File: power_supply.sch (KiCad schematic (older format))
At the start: 72 parts, among them IC1 TPS54561DPRT, J2 PJ-202A

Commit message: Started placing main components on PCB. Change of RT battery model and USB flash connector
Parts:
- removed BAT1: BU1632SM, sc606-baseboard-footprints:BU1632SM, symbol sc606-baseboard:BU1632SM
- added BAT1: MS621FE-FL11E, sc606-baseboard-footprints:MS621FE-FL11E, symbol sc606-baseboard:MS621FE-FL11E
- gave numbers to parts that had none: 49
- renumbered C21 to C22, C22 to C23, C23 to C25, C24 to C28, C25 to C29, C26 to C30, D?1 to D2, J2 to J1, L1 to L2, R6 to R12, R7 to R13, R8 to R14, R9 to R15, R3 to R6, R5 to R9

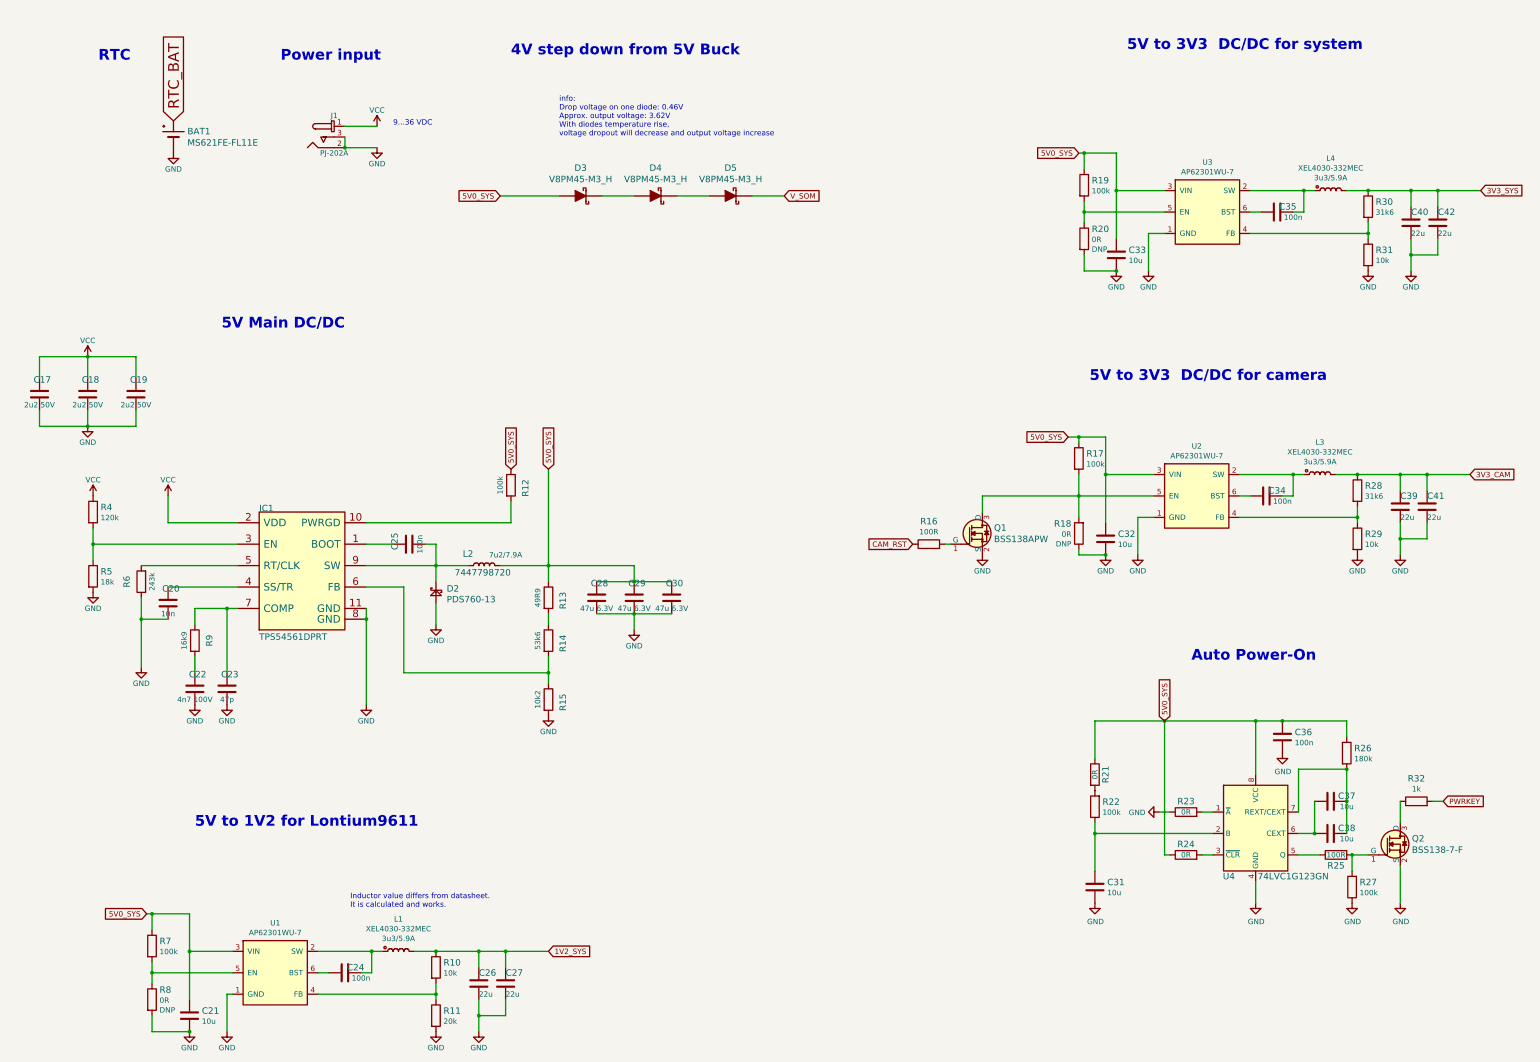
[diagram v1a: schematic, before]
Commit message: Changed USB flash and debug to USB-C. Prepared place for USB PD. Minor modifications of components position
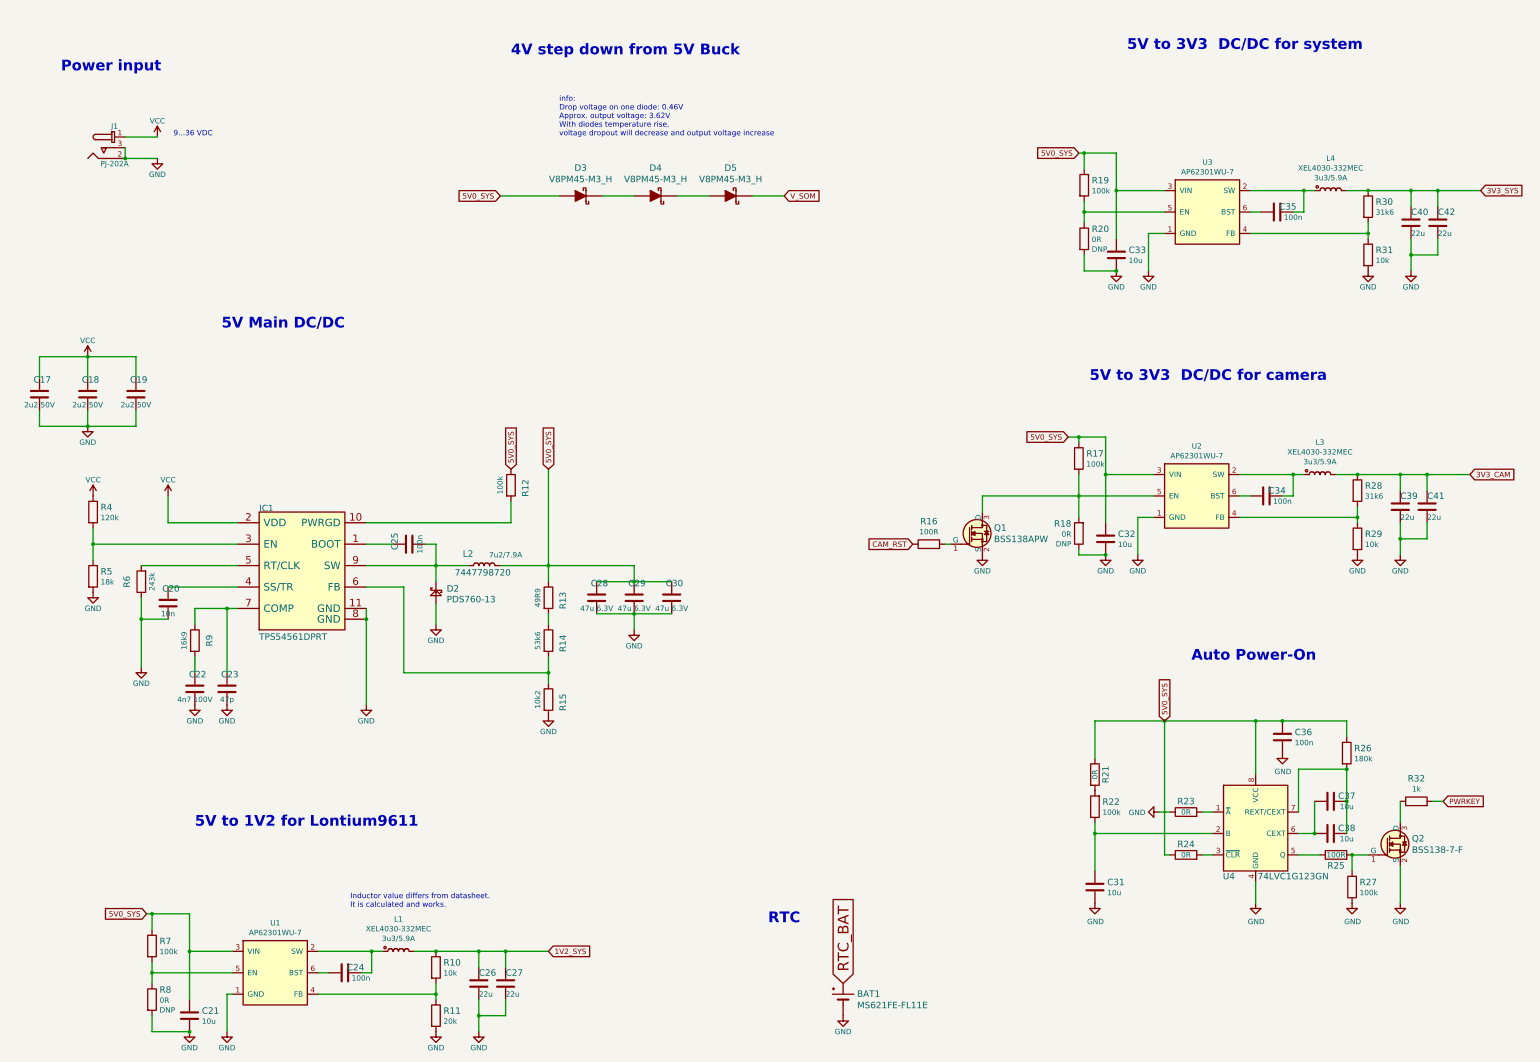
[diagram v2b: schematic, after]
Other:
- moved on the sheet: BAT1, J1
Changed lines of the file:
@@
 $Descr A3 16535 11693
 encoding utf-8
-Sheet 3 8
+Sheet 3 9
 Title ""
 Date "2022-01-04"
@@
 Comment4 ""
 $EndDescr
-Text Notes 1300 1150 0    100  ~ 20
+Text Notes 7550 9200 0    100  ~ 20
 RTC
 Text Notes 2450 3650 0    100  ~ 20
@@
 L sc606-baseboard:GND #PWR025
 U 1 1 623E5A47
-P 2000 2000
-F 0 "#PWR025" H 2000 1750 50  0001 C CNN
-F 1 "GND" H 2000 1850 50  0000 C CNN
-F 2 "" H 2000 2000 50  0001 C CNN
-F 3 "" H 2000 2000 50  0001 C CNN
-	1    2000 2000
-	1    0    0    -1
-$EndComp
-Text GLabel 2000 1700 1    100  Input ~ 0
+P 8250 10050
+F 0 "#PWR025" H 8250 9800 50  0001 C CNN
+F 1 "GND" H 8250 9900 50  0000 C CNN
+F 2 "" H 8250 10050 50  0001 C CNN
+F 3 "" H 8250 10050 50  0001 C CNN
+	1    8250 10050
+	1    0    0    -1
+$EndComp
+Text GLabel 8250 9750 1    100  Input ~ 0
 RTC_BAT
-Text Notes 3000 1150 0    100  ~ 20
+Text Notes 950  1250 0    100  ~ 20
 Power input
 $Comp
 L sc606-baseboard:PJ-202A J1
 U 1 1 623EC1D3
-P 3500 1750
-F 0 "J1" H 3500 1850 50  0000 C CNN
-F 1 "PJ-202A" H 3500 1500 50  0000 C CNN
-F 2 "sc606-baseboard-footprints:Barrel_Jack_5.5mmODx2.1mmID_PJ-202A" H 3700 1950 60  0001 L CNN
-F 3 "https://www.cui.com/product/resource/digikeypdf/pj-202a.pdf" H 3700 2050 60  0001 L CNN
-F 4 "CUI Inc." H 3700 2850 60  0001 L CNN "Manufacturer"
-F 5 "PJ-202A" H 3700 2250 60  0001 L CNN "MPN"
-	1    3500 1750
+P 1450 1850
+F 0 "J1" H 1450 1950 50  0000 C CNN
+F 1 "PJ-202A" H 1450 1600 50  0000 C CNN
+F 2 "sc606-baseboard-footprints:Barrel_Jack_5.5mmODx2.1mmID_PJ-202A" H 1650 2050 60  0001 L CNN
+F 3 "https://www.cui.com/product/resource/digikeypdf/pj-202a.pdf" H 1650 2150 60  0001 L CNN
+F 4 "CUI Inc." H 1650 2950 60  0001 L CNN "Manufacturer"
+F 5 "PJ-202A" H 1650 2350 60  0001 L CNN "MPN"
+	1    1450 1850
 	1    0    0    -1
 $EndComp
@@
 L sc606-baseboard:GND #PWR032
 U 1 1 623ECF5D
-P 3900 1950
-F 0 "#PWR032" H 3900 1700 50  0001 C CNN
-F 1 "GND" H 3900 1800 50  0000 C CNN
-F 2 "" H 3900 1950 50  0001 C CNN
-F 3 "" H 3900 1950 50  0001 C CNN
-	1    3900 1950
-	1    0    0    -1
-$EndComp
-Wire Wire Line
-	3600 1850 3600 1950
-Wire Wire Line
-	3900 1950 3600 1950
-Connection ~ 3600 1950
+P 1850 2050
+F 0 "#PWR032" H 1850 1800 50  0001 C CNN
+F 1 "GND" H 1850 1900 50  0000 C CNN
+F 2 "" H 1850 2050 50  0001 C CNN
+F 3 "" H 1850 2050 50  0001 C CNN
+	1    1850 2050
+	1    0    0    -1
+$EndComp
+Wire Wire Line
+	1550 1950 1550 2050
+Wire Wire Line
+	1850 2050 1550 2050
+Connection ~ 1550 2050
 $Comp
 L sc606-baseboard:VCC #PWR031
 U 1 1 623EE843
-P 3900 1750
-F 0 "#PWR031" H 3900 1600 50  0001 C CNN
-F 1 "VCC" H 3900 1900 50  0000 C CNN
-F 2 "" H 3900 1750 50  0001 C CNN
-F 3 "" H 3900 1750 50  0001 C CNN
-	1    3900 1750
-	1    0    0    -1
-$EndComp
-Wire Wire Line
-	3900 1750 3600 1750
+P 1850 1850
+F 0 "#PWR031" H 1850 1700 50  0001 C CNN
+F 1 "VCC" H 1850 2000 50  0000 C CNN
+F 2 "" H 1850 1850 50  0001 C CNN
+F 3 "" H 1850 1850 50  0001 C CNN
+	1    1850 1850
+	1    0    0    -1
+$EndComp
+Wire Wire Line
+	1850 1850 1550 1850
 $Comp
 L sc606-baseboard:VCC #PWR019
@@
 	0    1    1    0
 $EndComp
-Text Notes 4050 1750 0    50   ~ 0
+Text Notes 2000 1850 0    50   ~ 0
 9...36 VDC
 $Comp
@@
 L sc606-baseboard:MS621FE-FL11E BAT1
 U 1 1 61FDEF37
-P 2000 1800
-F 0 "BAT1" H 2130 1803 60  0000 L CNN
-F 1 "MS621FE-FL11E" H 2130 1697 60  0000 L CNN
-F 2 "sc606-baseboard-footprints:MS621FE-FL11E" H 2000 1800 60  0001 C CNN
-F 3 "" H 2000 1800 60  0001 C CNN
-F 4 "Seiko" H 2000 1800 50  0001 C CNN "Manufacturer"
-F 5 "MS621FE-FL11E" H 2000 1800 50  0001 C CNN "MPN"
-	1    2000 1800
-	1    0    0    -1
-$EndComp
+P 8250 9850
+F 0 "BAT1" H 8380 9853 60  0000 L CNN
+F 1 "MS621FE-FL11E" H 8380 9747 60  0000 L CNN
+F 2 "sc606-baseboard-footprints:MS621FE-FL11E" H 8250 9850 60  0001 C CNN
+F 3 "" H 8250 9850 60  0001 C CNN
+F 4 "Seiko" H 8250 9850 50  0001 C CNN "Manufacturer"
+F 5 "MS621FE-FL11E" H 8250 9850 50  0001 C CNN "MPN"
+	1    8250 9850
+	1    0    0    -1
+$EndComp

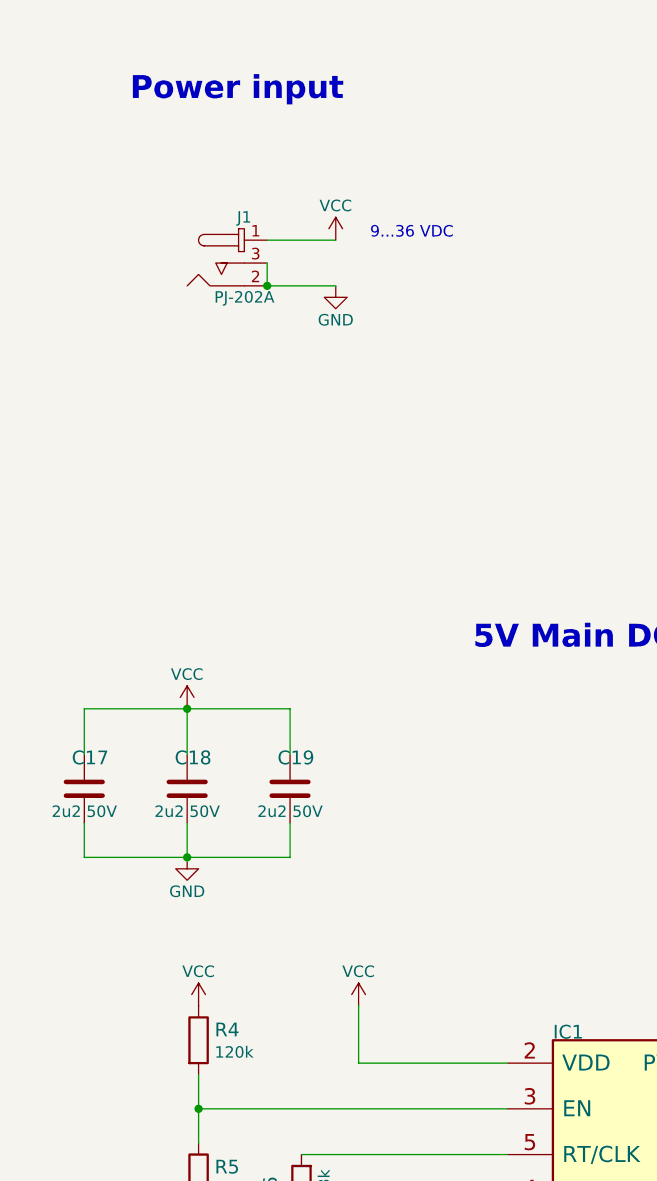
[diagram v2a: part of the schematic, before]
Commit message: Connected USB-PD and power select chip
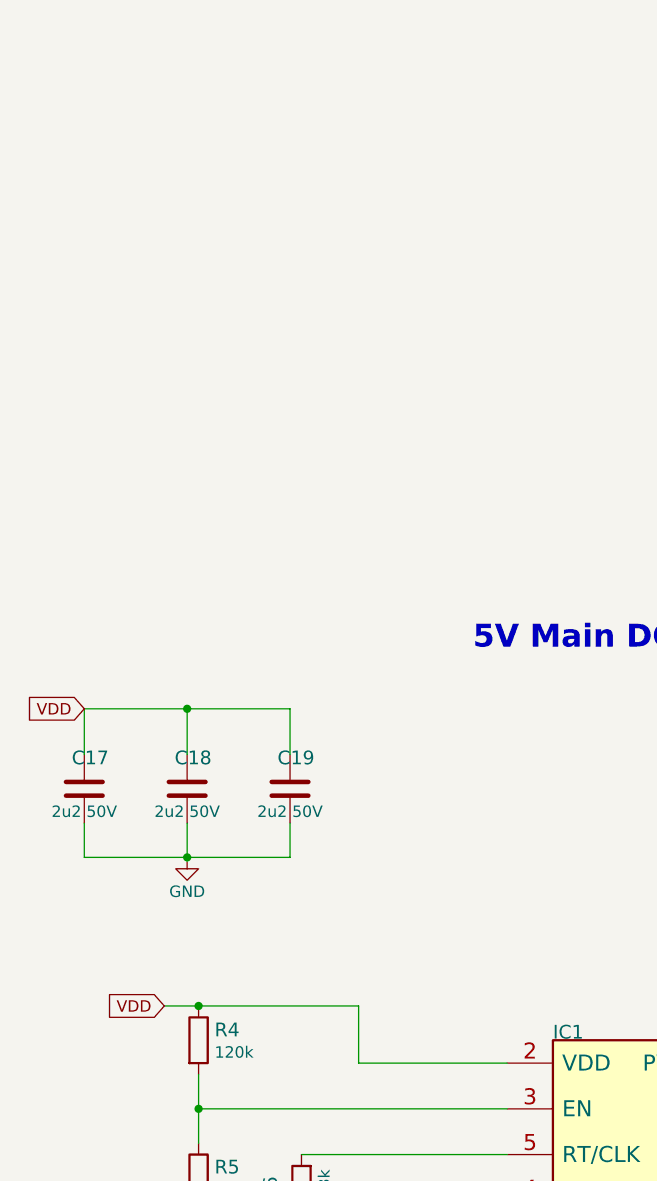
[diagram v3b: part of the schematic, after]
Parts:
- removed J1: PJ-202A, sc606-baseboard-footprints:Barrel_Jack_5.5mmODx2.1mmID_PJ-202A, symbol sc606-baseboard:PJ-202A
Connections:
- net VCC renamed VDD
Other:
- note removed: "9...36 VDC"
- note removed: "Power input"
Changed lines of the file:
@@
 Text GLabel 8250 9750 1    100  Input ~ 0
 RTC_BAT
-Text Notes 950  1250 0    100  ~ 20
-Power input
-$Comp
-L sc606-baseboard:PJ-202A J1
-U 1 1 623EC1D3
-P 1450 1850
-F 0 "J1" H 1450 1950 50  0000 C CNN
-F 1 "PJ-202A" H 1450 1600 50  0000 C CNN
-F 2 "sc606-baseboard-footprints:Barrel_Jack_5.5mmODx2.1mmID_PJ-202A" H 1650 2050 60  0001 L CNN
-F 3 "https://www.cui.com/product/resource/digikeypdf/pj-202a.pdf" H 1650 2150 60  0001 L CNN
-F 4 "CUI Inc." H 1650 2950 60  0001 L CNN "Manufacturer"
-F 5 "PJ-202A" H 1650 2350 60  0001 L CNN "MPN"
-	1    1450 1850
-	1    0    0    -1
-$EndComp
-$Comp
-L sc606-baseboard:GND #PWR032
-U 1 1 623ECF5D
-P 1850 2050
-F 0 "#PWR032" H 1850 1800 50  0001 C CNN
-F 1 "GND" H 1850 1900 50  0000 C CNN
-F 2 "" H 1850 2050 50  0001 C CNN
-F 3 "" H 1850 2050 50  0001 C CNN
-	1    1850 2050
-	1    0    0    -1
-$EndComp
-Wire Wire Line
-	1550 1950 1550 2050
-Wire Wire Line
-	1850 2050 1550 2050
-Connection ~ 1550 2050
-$Comp
-L sc606-baseboard:VCC #PWR031
-U 1 1 623EE843
-P 1850 1850
-F 0 "#PWR031" H 1850 1700 50  0001 C CNN
-F 1 "VCC" H 1850 2000 50  0000 C CNN
-F 2 "" H 1850 1850 50  0001 C CNN
-F 3 "" H 1850 1850 50  0001 C CNN
-	1    1850 1850
-	1    0    0    -1
-$EndComp
-Wire Wire Line
-	1850 1850 1550 1850
-$Comp
-L sc606-baseboard:VCC #PWR019
-U 1 1 623F5F58
-P 1200 3900
-F 0 "#PWR019" H 1200 3750 50  0001 C CNN
-F 1 "VCC" H 1200 4050 50  0000 C CNN
-F 2 "" H 1200 3900 50  0001 C CNN
-F 3 "" H 1200 3900 50  0001 C CNN
-	1    1200 3900
-	1    0    0    -1
-$EndComp
 $Comp
 L sc606-baseboard:GND #PWR020
@@
 F 5 "TPS54561DPRT" H 3200 5850 50  0001 C CNN "MPN"
 	1    3200 5850
-	1    0    0    -1
-$EndComp
-$Comp
-L sc606-baseboard:VCC #PWR024
-U 1 1 623FDB89
-P 1950 5200
-F 0 "#PWR024" H 1950 5050 50  0001 C CNN
-F 1 "VCC" H 1950 5350 50  0000 C CNN
-F 2 "" H 1950 5200 50  0001 C CNN
-F 3 "" H 1950 5200 50  0001 C CNN
-	1    1950 5200
 	1    0    0    -1
 $EndComp
@@
 	0    1    1    0
 $EndComp
-Text Notes 2000 1850 0    50   ~ 0
-9...36 VDC
 $Comp
 L sc606-baseboard:C_10u_0402 C33
@@
 Text Notes 3650 9050 0    50   ~ 0
 Inductor value differs from datasheet.\nIt is calculated and works.
-$Comp
-L sc606-baseboard:VCC #PWR021
-U 1 1 620D943B
-P 1250 5200
-F 0 "#PWR021" H 1250 5050 50  0001 C CNN
-F 1 "VCC" H 1250 5350 50  0000 C CNN
-F 2 "" H 1250 5200 50  0001 C CNN
-F 3 "" H 1250 5200 50  0001 C CNN
-	1    1250 5200
-	1    0    0    -1
-$EndComp
 $Comp
 L sc606-baseboard:GND #PWR022
@@
 	1    0    0    -1
 $EndComp
+Wire Wire Line
+	1950 5200 1250 5200
+Text GLabel 1100 5200 0    50   Input ~ 0
+VDD
+Wire Wire Line
+	1100 5200 1250 5200
+Connection ~ 1250 5200
+Text GLabel 750  3900 0    50   Input ~ 0
+VDD
 $EndSCHEMATC
